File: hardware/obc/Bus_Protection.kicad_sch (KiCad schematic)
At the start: 53 parts, among them Q11 MMDT2907, Q12 BSS138DWQ-7, Q13 BSS138DWQ-7, Q15 MBT2222ADW1T1, Q16 MBT2222ADW1T1, Q17 MMBT2907, Q18 BSS138DWQ-7, Q19 BSS138DWQ-7, Q7 MBT2222ADW1T1, Q8 MBT2222ADW1T1

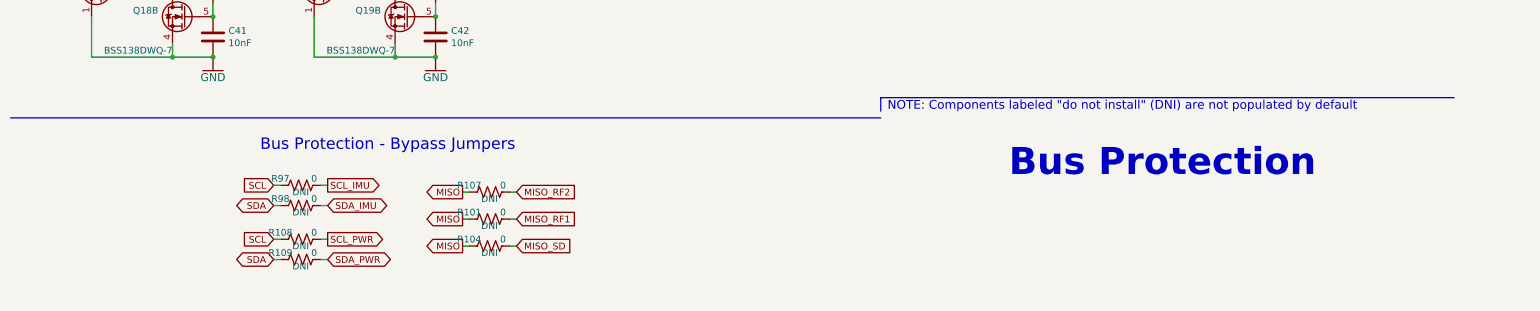
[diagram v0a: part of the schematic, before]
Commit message: obc: Schematic pages to US Letter (except Power)
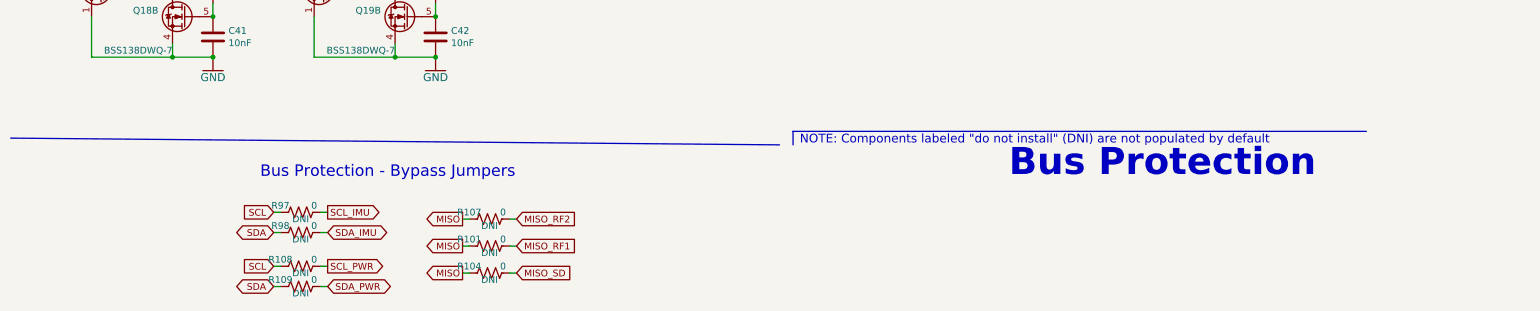
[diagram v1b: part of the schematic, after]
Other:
- moved on the sheet: R101, R104, R107, R108, R109, R97, R98

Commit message: obc: Add many XXX comments documenting 5/3 review
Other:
- note added: "I2C Bus Protection - Stacking"
- note added: "XXX Add another instance of the bus protection, producing SCL_STK and SDA_STK. Add those two signals to the stacking connector."
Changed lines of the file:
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@@
 	(polyline
 		(pts
-			(xy 181.61 66.04) (xy 115.57 66.04)
+			(xy 180.34 35.56) (xy 114.3 35.56)
 		)
 		(stroke
@@
 	(polyline
 		(pts
-			(xy 115.57 66.04) (xy 115.57 119.38)
+			(xy 114.3 35.56) (xy 114.3 88.9)
 		)
 		(stroke
@@
 	(polyline
 		(pts
-			(xy 181.61 119.38) (xy 181.61 66.04)
+			(xy 180.34 88.9) (xy 180.34 35.56)
 		)
 		(stroke
@@
 	(polyline
 		(pts
-			(xy 115.57 119.38) (xy 181.61 119.38)
+			(xy 114.3 88.9) (xy 180.34 88.9)
 		)
 		(stroke
@@
 	(text "These novel bus protection circuits\nprevent traditional I2C/SPI failure \nmodes where a single slave failure\ncan disable the entire bus.\n\nLearn more: \nhttps://doi.org/10.36227/techrxiv.15166620\n\nBy default, slave clock and/or data lines \ncan be held low and the Master (SAMD51) \nwill still be able to communicate with the \nremainder of the bus.\n\nThey can individually be bypassed by \nremoving the transistor(s) and soldering\nthe 0ohm the jumpers below."
 		(exclude_from_sim no)
-		(at 119.38 116.84 0)
+		(at 118.11 86.36 0)
 		(effects
 			(font
@@
 	(text "NOTE"
 		(exclude_from_sim no)
-		(at 116.84 71.12 0)
+		(at 115.57 40.64 0)
 		(effects
 			(font
@@
 		)
 	)
+	(text "I2C Bus Protection - Stacking"
+		(exclude_from_sim no)
+		(at 120.142 94.488 0)
+		(effects
+			(font
+				(size 2.159 2.159)
+			)
+			(justify left bottom)
+		)
+	)
 	(text "I2C Bus Protection - IMU"
 		(exclude_from_sim no)
@@
 		)
 	)
+	(text "XXX Add another instance of the bus protection,\nproducing SCL_STK and SDA_STK.\n\nAdd those two signals to the stacking connector."
+		(exclude_from_sim no)
+		(at 147.574 106.426 0)
+		(effects
+			(font
+				(size 1.27 1.27)
+			)
+		)
+	)

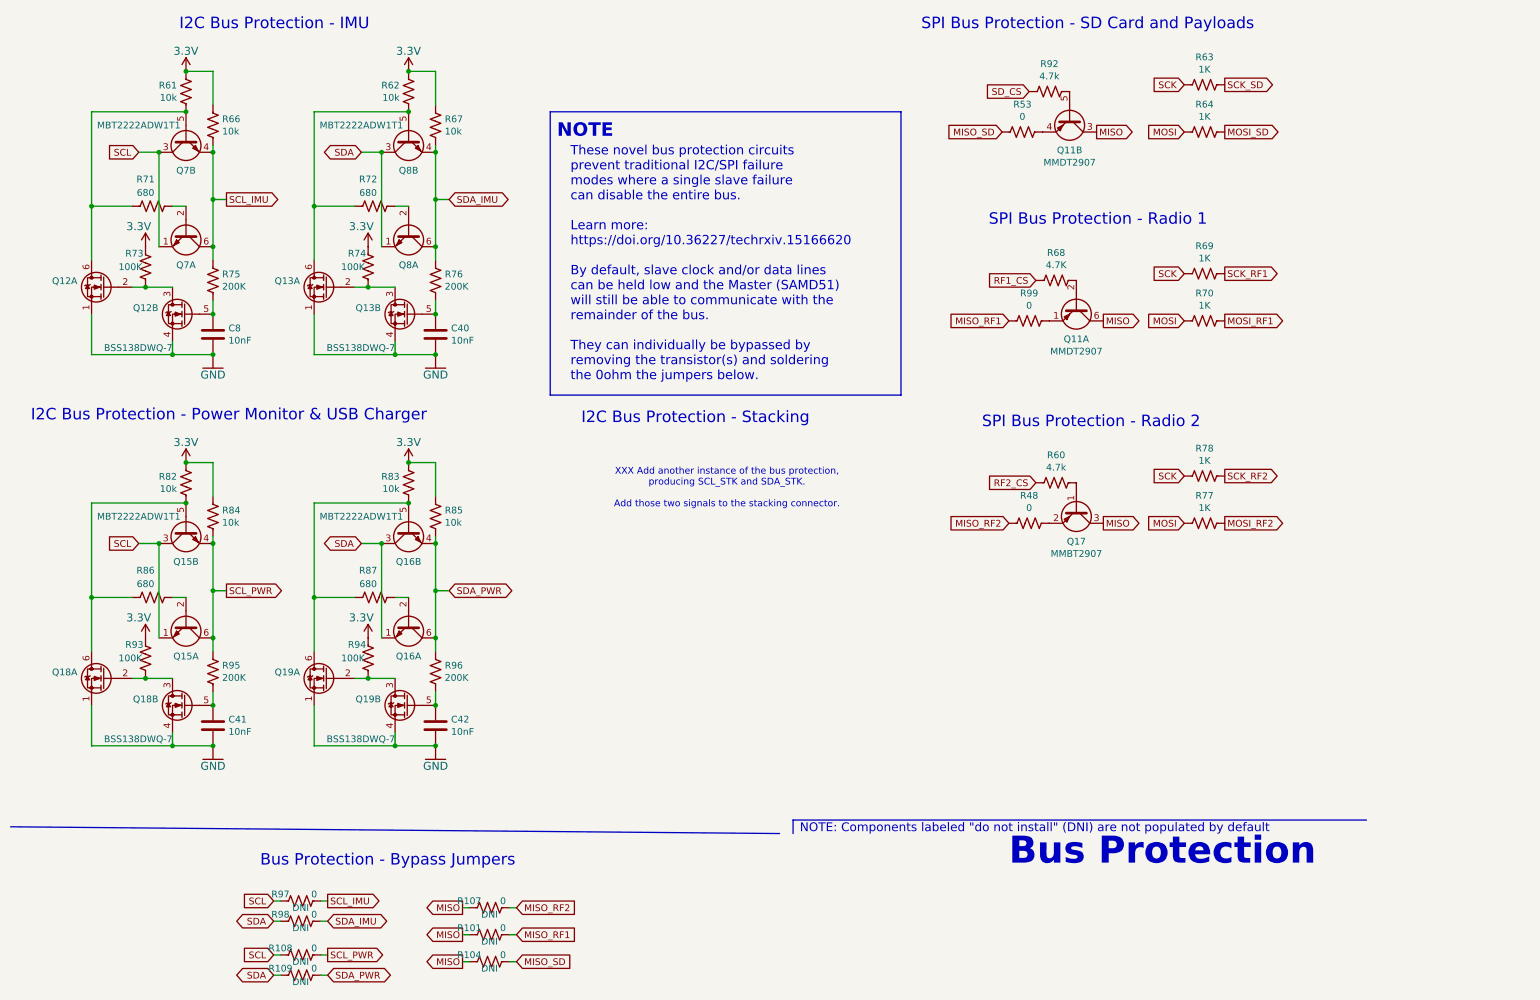
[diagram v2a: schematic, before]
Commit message: obc: schematic cleanup and wiring
Demarcated NC pins, added High-Rel connectors, cleaned up schematic legibility, and added bus protection for stacking signals SDA & SCL.
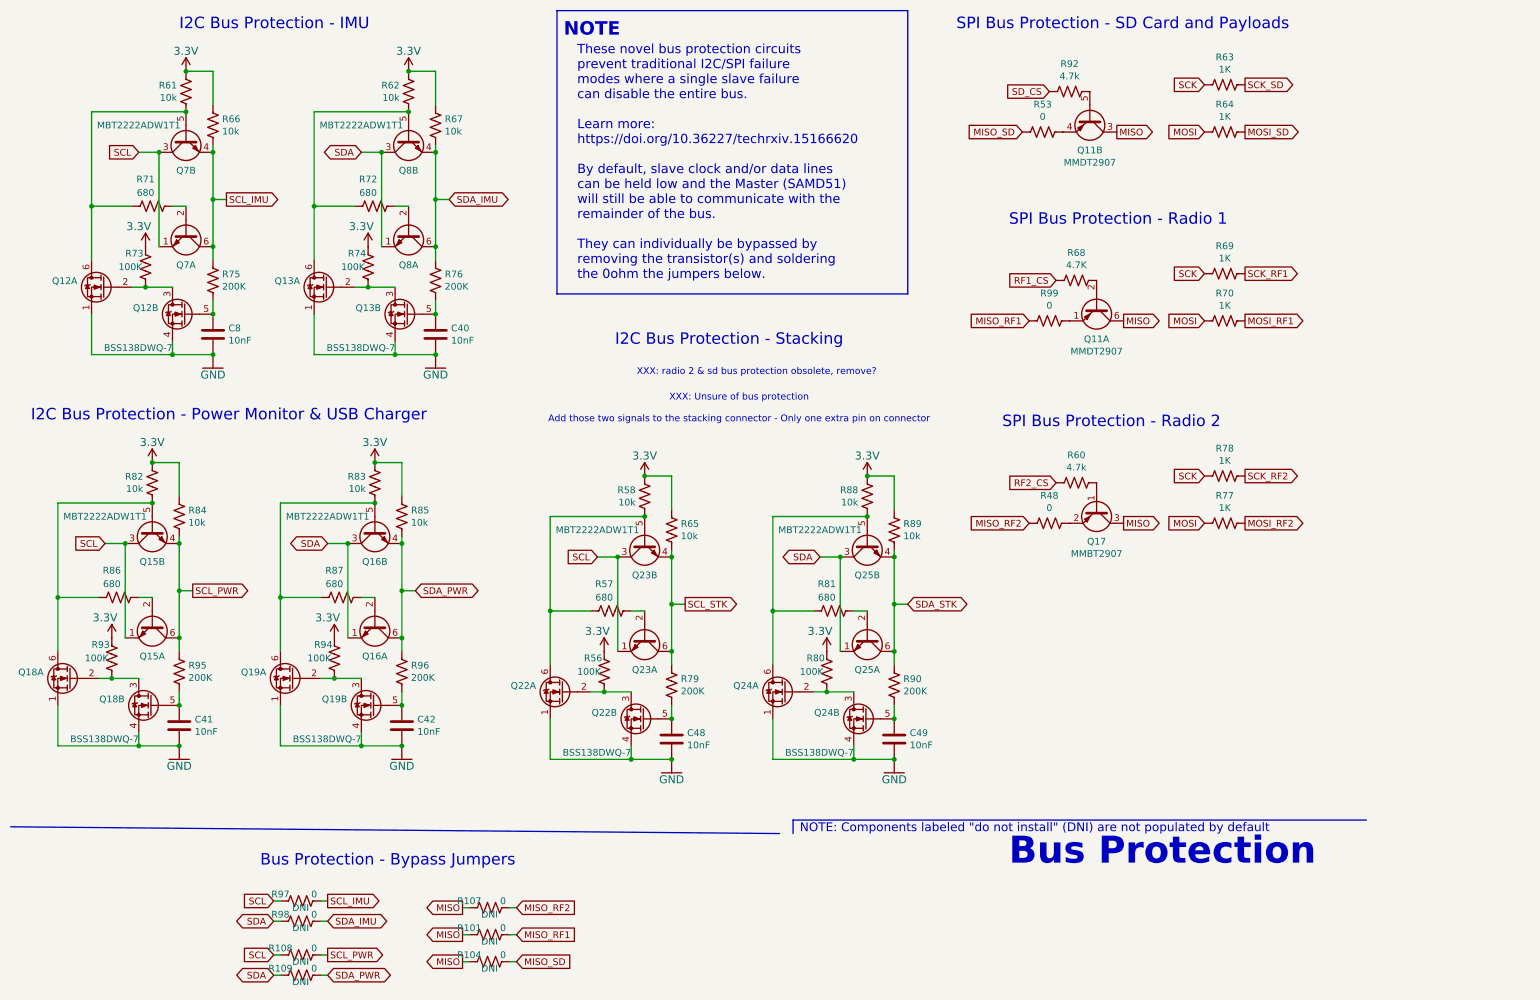
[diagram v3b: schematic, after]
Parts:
- added C48, C49: 10nF, Capacitor_SMD:C_0603_1608Metric, symbol Device:C
- added Q22, Q24: BSS138DWQ-7, mainboard:BSS138DWQ-7, symbol mainboard:BSS138DWQ-7
- added Q23, Q25: MBT2222ADW1T1, Package_TO_SOT_SMD:SOT-363_SC-70-6, symbol Transistor_BJT:MBT2222ADW1T1
- added R56, R80: 100K, Resistor_SMD:R_0603_1608Metric, symbol Device:R_US
- added R57, R81: 680, Resistor_SMD:R_0603_1608Metric, symbol Device:R_US
- added R58, R65, R88, R89: 10k, Resistor_SMD:R_0603_1608Metric, symbol Device:R_US
- added R79, R90: 200K, Resistor_SMD:R_0603_1608Metric, symbol Device:R_US
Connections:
- net 3.3V: now also R56.1, R58.1, R65.1, R80.1, R88.1, R89.1
- net GND: now also C48.2, C49.2, Q22.1 (S2), Q22.4 (S1), Q24.1 (S2), Q24.4 (S1)
- net SCL: now also Q23.1 (E1), Q23.3 (C2)
- net SDA: now also Q25.1 (E1), Q25.3 (C2)
- new net: C49.1, Q24.5 (G1), R90.2
- new net: Q22.6 (D1), Q23.5 (B2), R57.2, R58.2
- new net: Q22.2 (G2), Q22.3 (D2), R56.2
- new net: Q23.2 (B1), R57.1
- new net: Q25.2 (B1), R81.1
- new net: Q24.6 (D1), Q25.5 (B2), R81.2, R88.2
- new net: C48.1, Q22.5 (G1), R79.2
- new net: Q24.2 (G2), Q24.3 (D2), R80.2
- new net SCL_STK: Q23.4 (E2), Q23.6 (C1), R65.2, R79.1
- new net SDA_STK: Q25.4 (E2), Q25.6 (C1), R89.2, R90.1
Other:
- note added: "XXX: Unsure of bus protection Add those two signals to the stacking connector - Only one extra pin on connector"
- note added: "XXX: radio 2 & sd bus protection obsolete, remove?"
- note removed: "XXX Add another instance of the bus protection, producing SCL_STK and SDA_STK. Add those two signals to the stacking connector."
- moved on the sheet: C41, C42, Q11A, Q11B, Q15A, Q15B, Q16A, Q16B, Q17, Q18A, Q18B, Q19A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

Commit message: obc: schematic editing and footprint development
Deleted irrelevant SD-related circuits and pins. Created new & modified existing connector and inductor footprints. Added new components (Bat Charger, High-Rel Connector, etc.)
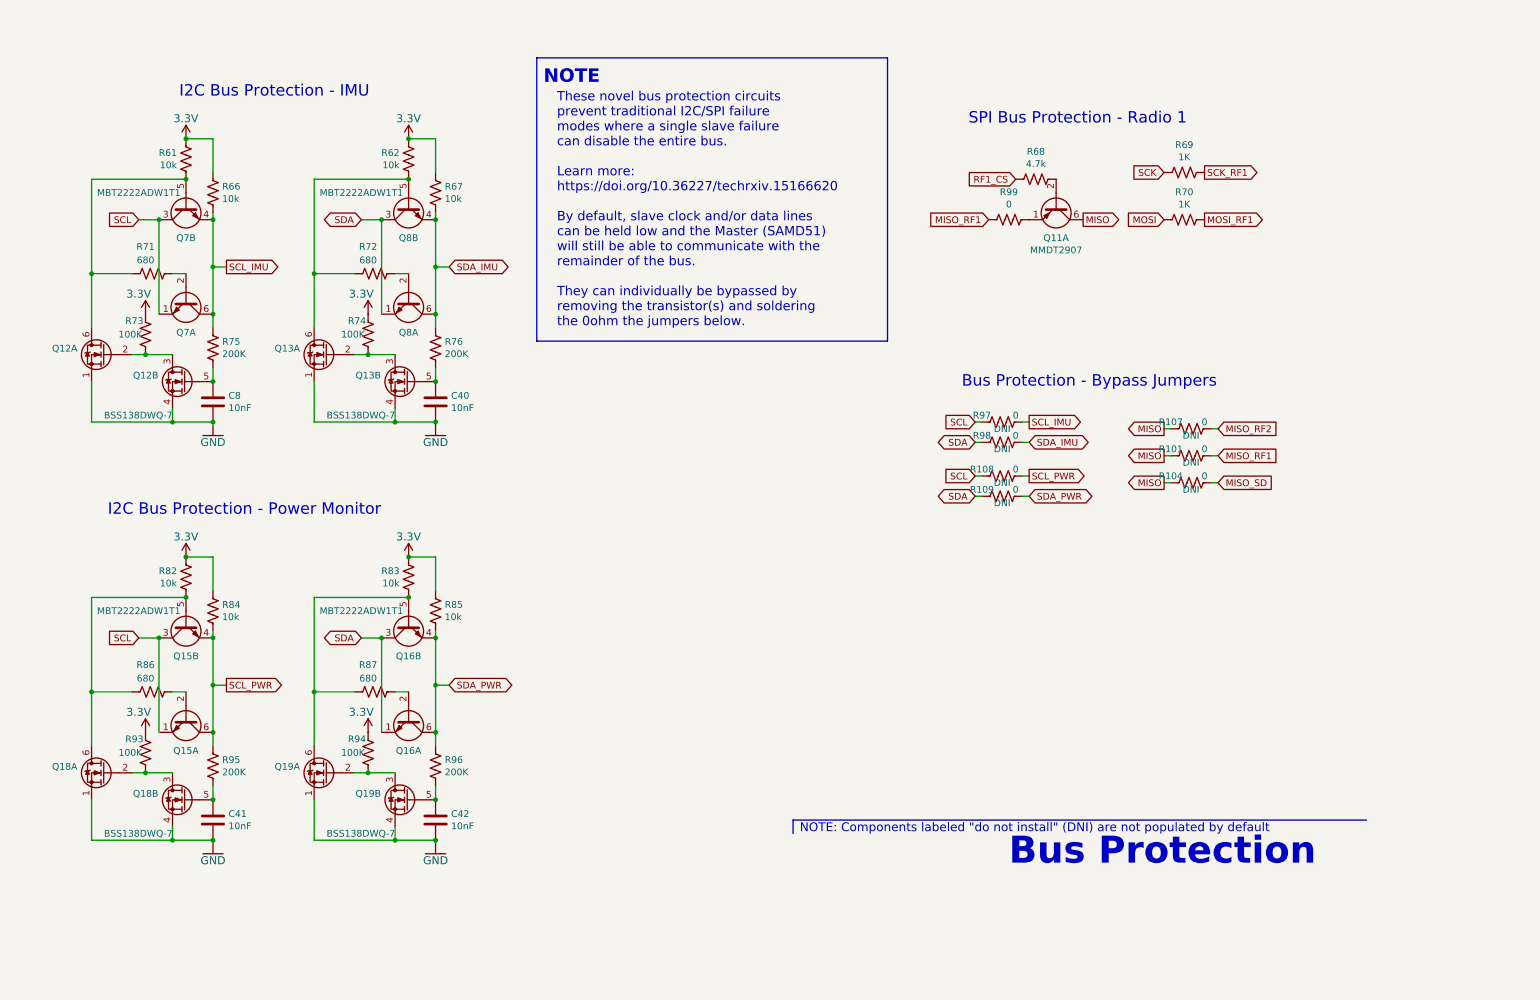
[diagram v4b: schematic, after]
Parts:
- removed C48, C49: 10nF, Capacitor_SMD:C_0603_1608Metric, symbol Device:C
- removed unit 2 of Q11
- removed Q17: MMBT2907, Package_TO_SOT_SMD:SOT-23, symbol mainboard:MMBT2907
- removed Q22, Q24: BSS138DWQ-7, mainboard:BSS138DWQ-7, symbol mainboard:BSS138DWQ-7
- removed Q23, Q25: MBT2222ADW1T1, Package_TO_SOT_SMD:SOT-363_SC-70-6, symbol Transistor_BJT:MBT2222ADW1T1
- removed R48, R53: 0, Resistor_SMD:R_0603_1608Metric, symbol Device:R_US
- removed R56, R80: 100K, Resistor_SMD:R_0603_1608Metric, symbol Device:R_US
- removed R57, R81: 680, Resistor_SMD:R_0603_1608Metric, symbol Device:R_US
- removed R58, R65, R88, R89: 10k, Resistor_SMD:R_0603_1608Metric, symbol Device:R_US
- removed R60, R92: 4.7k, Resistor_SMD:R_0603_1608Metric, symbol Device:R_US
- removed R63, R64, R77, R78: 1K, Resistor_SMD:R_0603_1608Metric, symbol Device:R_US
- removed R79, R90: 200K, Resistor_SMD:R_0603_1608Metric, symbol Device:R_US
- R68: value 4.7K -> 4.7k
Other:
- note added: "I2C Bus Protection - Power Monitor"
- note removed: "I2C Bus Protection - Power Monitor & USB Charger"
- note removed: "I2C Bus Protection - Stacking"
- note removed: "SPI Bus Protection - Radio 2"
- note removed: "SPI Bus Protection - SD Card and Payloads"
- note removed: "XXX: Unsure of bus protection Add those two signals to the stacking connector - Only one extra pin on connector"
- note removed: "XXX: radio 2 & sd bus protection obsolete, remove?"
- moved on the sheet: C40, C41, C42, C8, Q11A, Q12A, Q12B, Q13A, Q13B, Q15A, Q15B, Q16A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

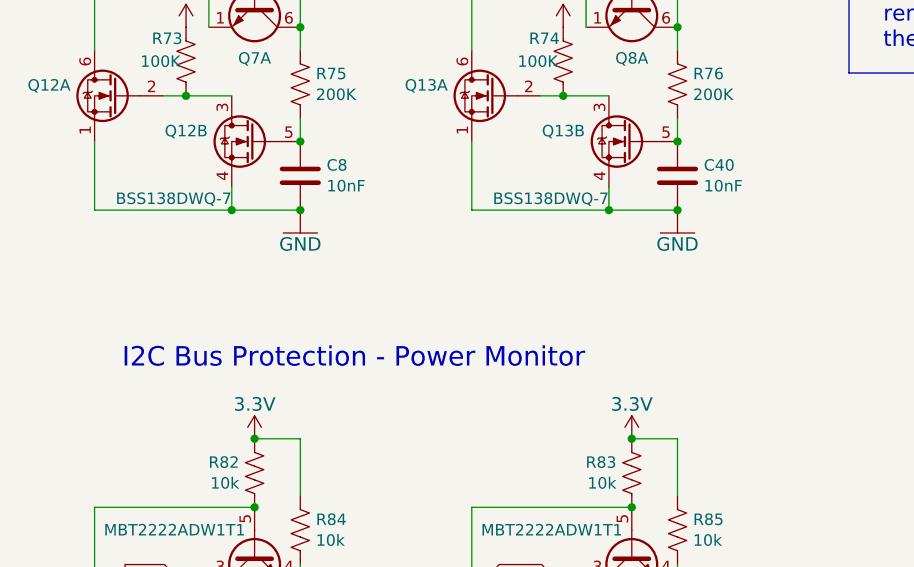
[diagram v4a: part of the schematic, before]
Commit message: obc: BOM component verification
Verified part numbers, availability, values, footprints, etc. of components. Next steps involve verifying footprints and potentially researching some alternative components.
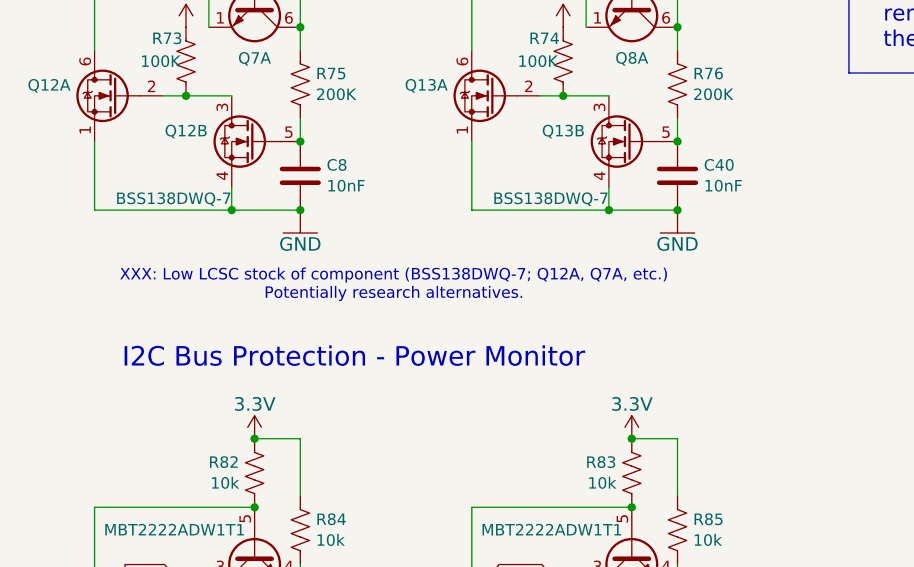
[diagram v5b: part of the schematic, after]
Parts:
- Q12, Q13, Q18, Q19: footprint mainboard:BSS138DWQ-7 -> Package_TO_SOT_SMD:SOT-363_SC-70-6
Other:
- note added: "XXX: Low LCSC stock of component (BSS138DWQ-7; Q12A, Q7A, etc.) Potentially research alternatives."
